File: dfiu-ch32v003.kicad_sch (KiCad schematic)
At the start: 46 parts, among them J1 Conn_01x03_Pin, J2 SAO, Q1 SI2302-HXY, Q2 SI2302-HXY, U1 CH32V003FxUx

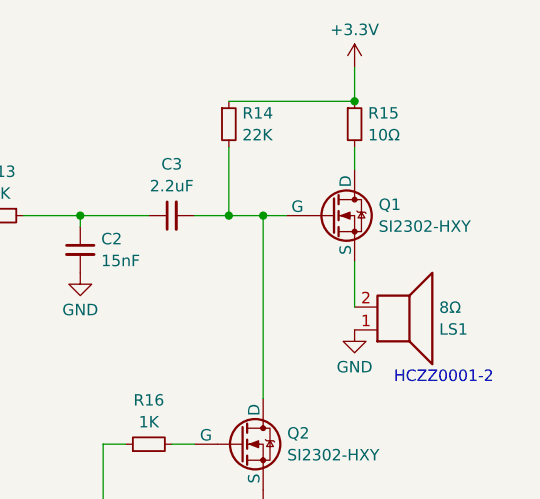
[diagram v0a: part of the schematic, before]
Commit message: updated part number for Q1
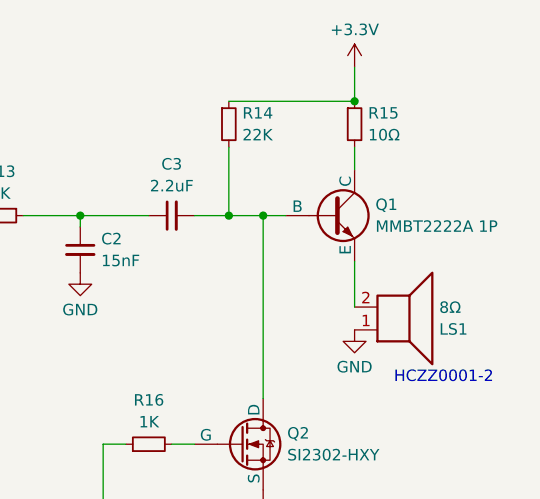
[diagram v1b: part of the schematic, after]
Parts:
- Q1: value SI2302-HXY -> MMBT2222A 1P; symbol Simulation_SPICE:NMOS -> Simulation_SPICE:NPN
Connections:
- net at LS1.2: now also Q1.3 (E); no longer Q1.S
- net at R15.2: now also Q1.1 (C); no longer Q1.D
- net at C3.2, Q2.D, R14.2: now also Q1.2 (B); no longer Q1.G
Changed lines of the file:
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@@
 	)
 	(symbol
-		(lib_id "Simulation_SPICE:NMOS")
+		(lib_id "Simulation_SPICE:NPN")
 		(at 238.76 45.72 0)
 		(unit 1)
@@
 		(fields_autoplaced yes)
 		(property "Reference" "Q1"
-			(at 243.967 44.5078 0)
+			(at 243.6114 44.5078 0)
 			(effects
 				(font
@@
 			)
 		)
-		(property "Value" "SI2302-HXY"
-			(at 243.967 46.9321 0)
+		(property "Value" "MMBT2222A 1P"
+			(at 243.6114 46.9321 0)
 			(effects
 				(font
@@
 		)
 		(property "Footprint" "Package_TO_SOT_SMD:SOT-23"
-			(at 243.84 43.18 0)
+			(at 302.26 45.72 0)
 			(effects
 				(font
@@
 			)
 		)
-		(property "Datasheet" "https://ngspice.sourceforge.io/docs/ngspice-html-manual/manual.xhtml#cha_MOSFETs"
-			(at 238.76 58.42 0)
+		(property "Datasheet" "https://ngspice.sourceforge.io/docs/ngspice-html-manual/manual.xhtml#cha_BJTs"
+			(at 302.26 45.72 0)
 			(effects
 				(font
@@
 			)
 		)
-		(property "Description" "N-MOSFET transistor, drain/source/gate"
+		(property "Description" "Bipolar transistor symbol for simulation only, substrate tied to the emitter"
 			(at 238.76 45.72 0)
 			(effects
@@
 			)
 		)
-		(property "Sim.Device" "NMOS"
-			(at 238.76 62.865 0)
+		(property "Sim.Device" "NPN"
+			(at 238.76 45.72 0)
 			(effects
 				(font
@@
 			)
 		)
-		(property "Sim.Type" "VDMOS"
-			(at 238.76 64.77 0)
+		(property "Sim.Type" "GUMMELPOON"
+			(at 238.76 45.72 0)
 			(effects
 				(font
@@
 			)
 		)
-		(property "Sim.Pins" "1=D 2=G 3=S"
-			(at 238.76 60.96 0)
+		(property "Sim.Pins" "1=C 2=B 3=E"
+			(at 238.76 45.72 0)
 			(effects
 				(font
@@
 			)
 		)
-		(pin "S"
+		(pin "3"
 		)
-		(pin "D"
+		(pin "1"
 		)
-		(pin "G"
+		(pin "2"
 		)
 		(instances
